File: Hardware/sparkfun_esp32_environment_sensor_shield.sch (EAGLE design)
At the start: 48 parts, among them J1 WEATHER_METER-WIND, J2 WEATHER_METER-RAIN, U1 BME280, U2 CCS811, U3 TSL2561FN, U4 ESD Diode

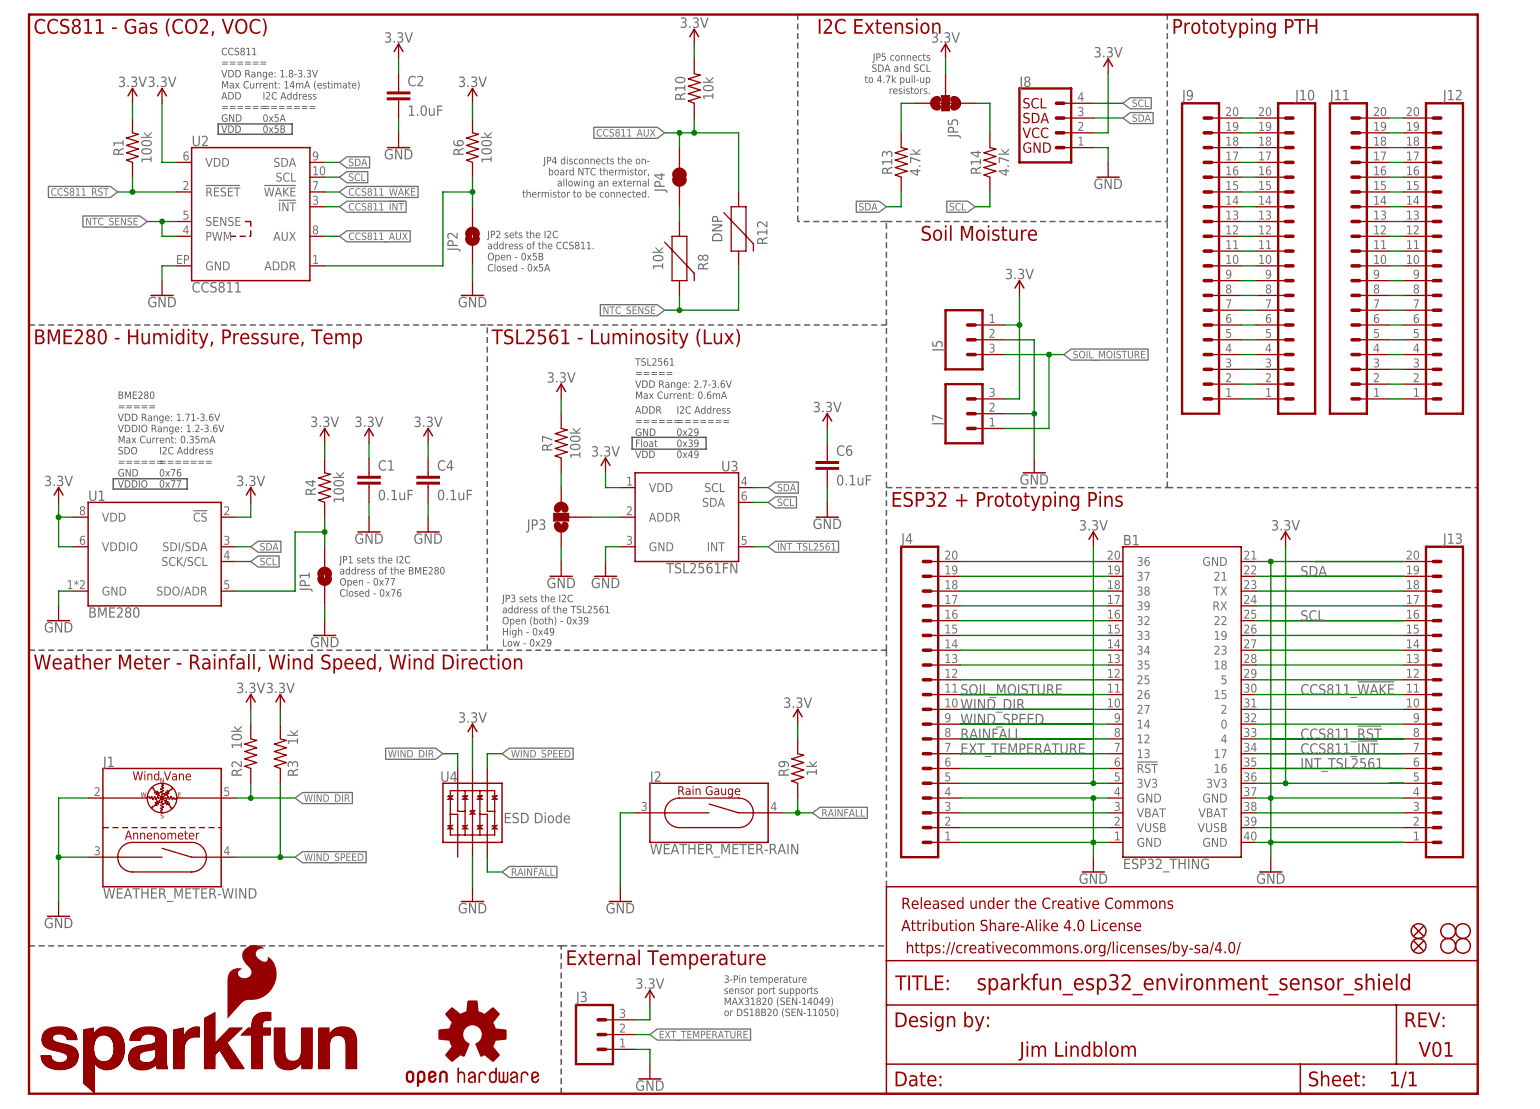
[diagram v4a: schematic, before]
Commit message: Post-review fixes: CCS811 paste, spell check
- Reduced size of CCS811's exposed pad paste aperature
- Fixed anemometer spelling
- Changed "Gas" to "Air" labels
- Clean up schematic
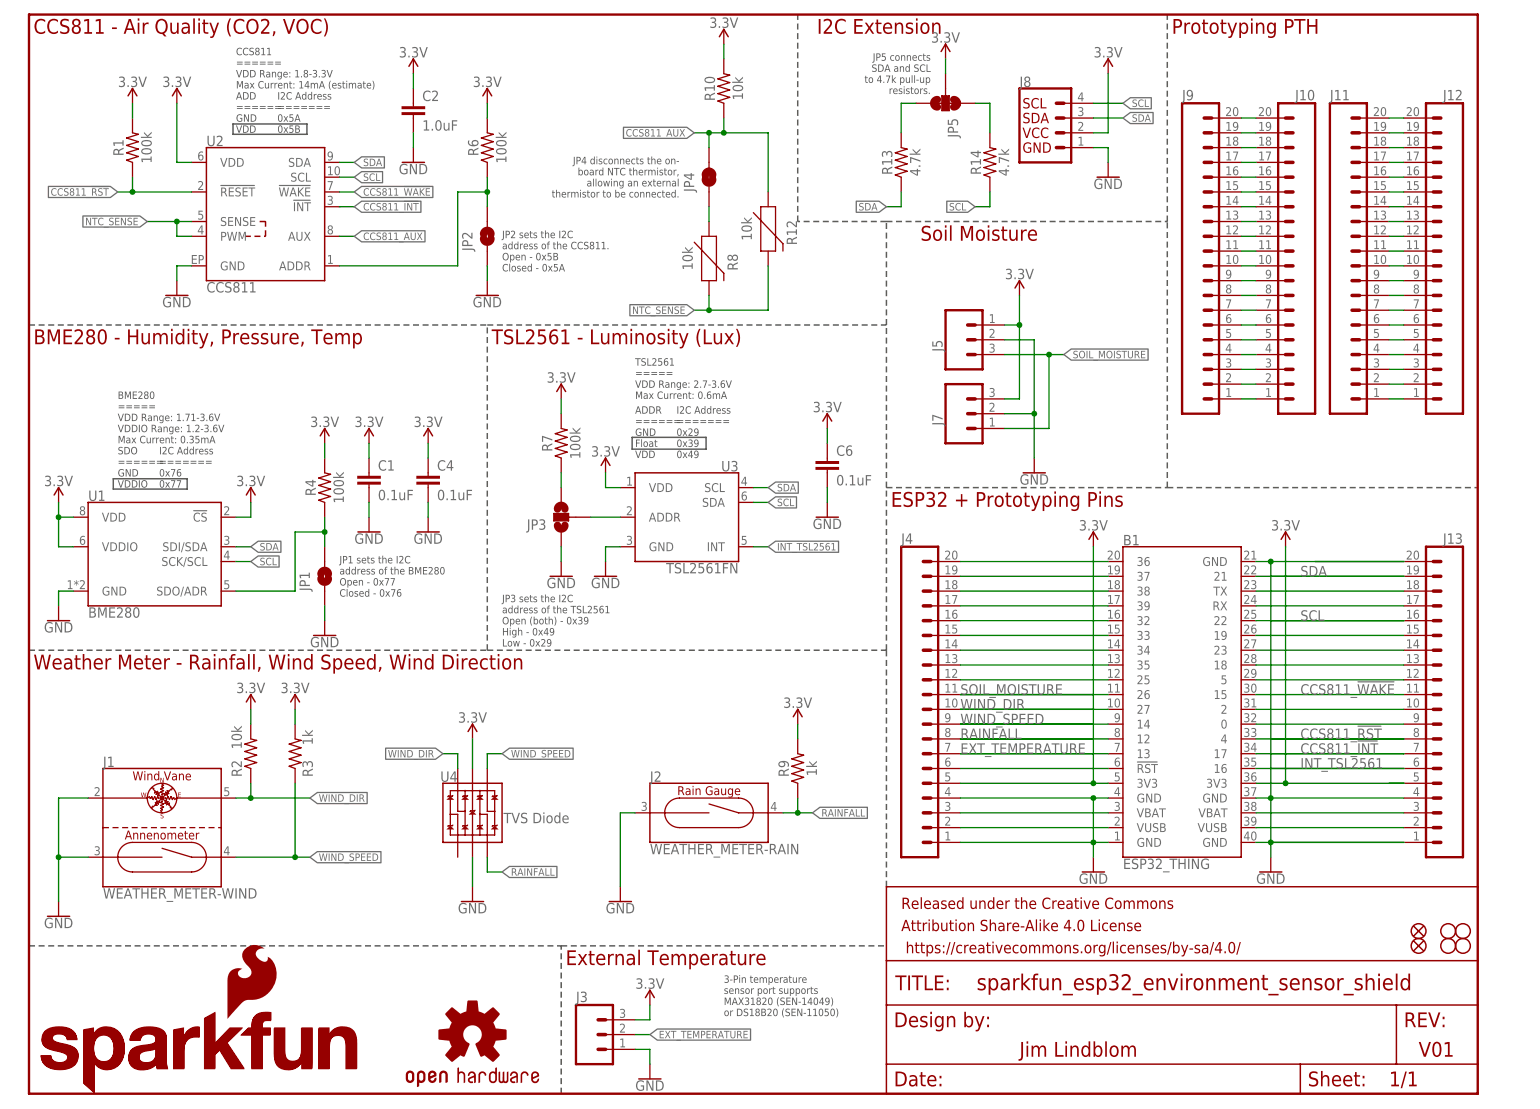
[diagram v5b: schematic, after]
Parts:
- R12: value DNP -> 10k
- U4: value ESD Diode -> TVS Diode
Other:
- note added: "CCS811 - Air Quality (CO2, VOC)"
- note removed: "CCS811 - Gas (CO2, VOC)"
- moved on the sheet: C2, JP2, JP4, R10, R12, R3, R6, R8, U2

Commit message: Minor adjustments after running Engineer checklist.
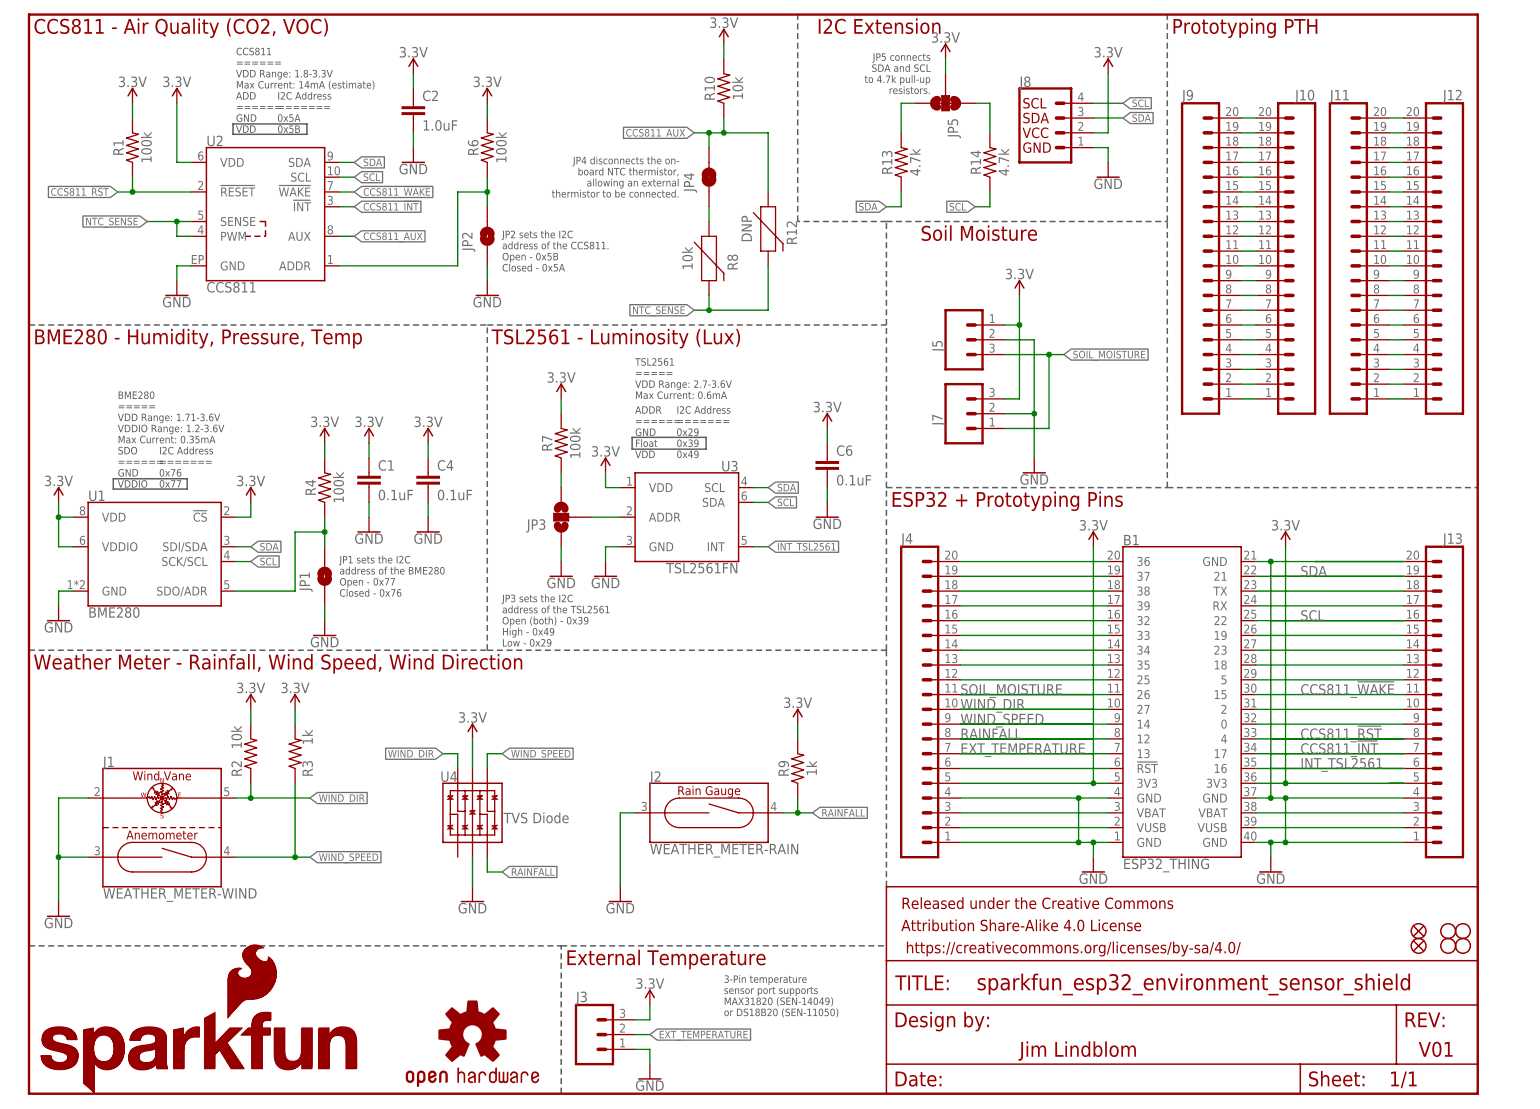
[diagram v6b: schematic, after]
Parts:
- added LOGO3: SFE_LOGO_FLAME.1_INCH, SparkFun-Aesthetics:SFE_LOGO_FLAME.1_INCH
- R12: value 10k -> DNP; PROD_ID (none) -> N/A
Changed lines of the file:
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@@
 <part name="JP5" library="SparkFun-Jumpers" deviceset="JUMPER-SMT_3_2-NC_TRACE" device="_SILK" value=""/>
 <part name="R8" library="esp32-environ-monitor-temp" deviceset="NTC-THERMISTOR" device="-0603" value="10k"/>
-<part name="R12" library="esp32-environ-monitor-temp" deviceset="NTC-THERMISTOR" device="-AXIAL-0.1" value="10k"/>
+<part name="R12" library="esp32-environ-monitor-temp" deviceset="NTC-THERMISTOR" device="-AXIAL-0.1" value="DNP">
+<attribute name="PROD_ID" value="N/A"/>
+</part>
 <part name="LOGO1" library="SparkFun-Aesthetics" deviceset="SFE_LOGO_NAME" device=".1_INCH"/>
 <part name="LOGO4" library="SparkFun-Aesthetics" deviceset="OSHW-LOGO" device="S"/>
@@
 <part name="SUPPLY23" library="SparkFun-PowerSymbols" deviceset="3.3V" device=""/>
 <part name="GND7" library="SparkFun-PowerSymbols" deviceset="GND" device=""/>
+<part name="LOGO3" library="SparkFun-Aesthetics" deviceset="SFE_LOGO_FLAME" device=".1_INCH"/>
 </parts>
 <sheets>
@@
 <instance part="SUPPLY23" gate="G$1" x="76.2" y="60.96"/>
 <instance part="GND7" gate="1" x="76.2" y="33.02" rot="MR0"/>
+<instance part="LOGO3" gate="G$1" x="33.782" y="12.446"/>
 </instances>
 <busses>
@@
 <nets>
 <net name="GND" class="0">
-<segment>
-<pinref part="GND17" gate="1" pin="GND"/>
-<pinref part="B1" gate="G$1" pin="GND@1"/>
-<pinref part="B1" gate="G$1" pin="GND@4"/>
-<pinref part="J4" gate="G$1" pin="1"/>
-<pinref part="J4" gate="G$1" pin="4"/>
-<wire x1="160.02" y1="43.18" x2="182.88" y2="43.18" width="0.1524" layer="91"/>
-<wire x1="182.88" y1="43.18" x2="185.42" y2="43.18" width="0.1524" layer="91"/>
-<wire x1="160.02" y1="50.8" x2="182.88" y2="50.8" width="0.1524" layer="91"/>
-<wire x1="182.88" y1="50.8" x2="185.42" y2="50.8" width="0.1524" layer="91"/>
-<wire x1="182.88" y1="40.64" x2="182.88" y2="43.18" width="0.1524" layer="91"/>
-<junction x="182.88" y="43.18"/>
-<wire x1="182.88" y1="43.18" x2="182.88" y2="50.8" width="0.1524" layer="91"/>
-<junction x="182.88" y="50.8"/>
-</segment>
-<segment>
-<pinref part="B1" gate="G$1" pin="GND@21"/>
-<wire x1="236.22" y1="91.44" x2="220.98" y2="91.44" width="0.1524" layer="91"/>
-<pinref part="J13" gate="G$1" pin="20"/>
-<wire x1="236.22" y1="91.44" x2="213.36" y2="91.44" width="0.1524" layer="91"/>
-<pinref part="B1" gate="G$1" pin="GND@40"/>
-<pinref part="GND19" gate="1" pin="GND"/>
-<wire x1="213.36" y1="91.44" x2="210.82" y2="91.44" width="0.1524" layer="91"/>
-<wire x1="236.22" y1="43.18" x2="213.36" y2="43.18" width="0.1524" layer="91"/>
-<wire x1="213.36" y1="43.18" x2="213.36" y2="40.64" width="0.1524" layer="91"/>
-<pinref part="B1" gate="G$1" pin="GND@37"/>
-<wire x1="213.36" y1="50.8" x2="213.36" y2="43.18" width="0.1524" layer="91"/>
-<junction x="213.36" y="43.18"/>
-<pinref part="J13" gate="G$1" pin="1"/>
-<pinref part="J13" gate="G$1" pin="4"/>
-<wire x1="236.22" y1="43.18" x2="210.82" y2="43.18" width="0.1524" layer="91"/>
-<wire x1="236.22" y1="50.8" x2="213.36" y2="50.8" width="0.1524" layer="91"/>
-<wire x1="213.36" y1="50.8" x2="210.82" y2="50.8" width="0.1524" layer="91"/>
-<wire x1="213.36" y1="91.44" x2="213.36" y2="50.8" width="0.1524" layer="91"/>
-<junction x="213.36" y="91.44"/>
-<junction x="213.36" y="50.8"/>
-</segment>
 <segment>
 <pinref part="GND3" gate="1" pin="GND"/>
@@
 <wire x1="76.2" y1="35.56" x2="76.2" y2="40.64" width="0.1524" layer="91"/>
 </segment>
+<segment>
+<pinref part="B1" gate="G$1" pin="GND@1"/>
+<pinref part="B1" gate="G$1" pin="GND@4"/>
+<pinref part="J4" gate="G$1" pin="1"/>
+<pinref part="J4" gate="G$1" pin="4"/>
+<wire x1="160.02" y1="43.18" x2="180.34" y2="43.18" width="0.1524" layer="91"/>
+<wire x1="180.34" y1="43.18" x2="182.88" y2="43.18" width="0.1524" layer="91"/>
+<wire x1="182.88" y1="43.18" x2="185.42" y2="43.18" width="0.1524" layer="91"/>
+<wire x1="160.02" y1="50.8" x2="180.34" y2="50.8" width="0.1524" layer="91"/>
+<wire x1="180.34" y1="50.8" x2="185.42" y2="50.8" width="0.1524" layer="91"/>
+<junction x="180.34" y="43.18"/>
+<wire x1="180.34" y1="43.18" x2="180.34" y2="50.8" width="0.1524" layer="91"/>
+<junction x="180.34" y="50.8"/>
+<pinref part="GND17" gate="1" pin="GND"/>
+<wire x1="182.88" y1="40.64" x2="182.88" y2="43.18" width="0.1524" layer="91"/>
+<junction x="182.88" y="43.18"/>
+</segment>
+<segment>
+<pinref part="B1" gate="G$1" pin="GND@40"/>
+<pinref part="J13" gate="G$1" pin="1"/>
+<wire x1="236.22" y1="43.18" x2="215.9" y2="43.18" width="0.1524" layer="91"/>
+<wire x1="215.9" y1="43.18" x2="213.36" y2="43.18" width="0.1524" layer="91"/>
+<wire x1="213.36" y1="43.18" x2="210.82" y2="43.18" width="0.1524" layer="91"/>
+<junction x="213.36" y="43.18"/>
+<pinref part="GND19" gate="1" pin="GND"/>
+<wire x1="213.36" y1="40.64" x2="213.36" y2="43.18" width="0.1524" layer="91"/>
+<pinref part="B1" gate="G$1" pin="GND@37"/>
+<pinref part="J13" gate="G$1" pin="4"/>
+<wire x1="236.22" y1="50.8" x2="215.9" y2="50.8" width="0.1524" layer="91"/>
+<pinref part="B1" gate="G$1" pin="GND@21"/>
+<wire x1="215.9" y1="50.8" x2="213.36" y2="50.8" width="0.1524" layer="91"/>
+<wire x1="213.36" y1="50.8" x2="210.82" y2="50.8" width="0.1524" layer="91"/>
+<wire x1="236.22" y1="91.44" x2="220.98" y2="91.44" width="0.1524" layer="91"/>
+<pinref part="J13" gate="G$1" pin="20"/>
+<wire x1="236.22" y1="91.44" x2="213.36" y2="91.44" width="0.1524" layer="91"/>
+<wire x1="213.36" y1="91.44" x2="210.82" y2="91.44" width="0.1524" layer="91"/>
+<wire x1="213.36" y1="91.44" x2="213.36" y2="50.8" width="0.1524" layer="91"/>
+<junction x="213.36" y="91.44"/>
+<junction x="213.36" y="50.8"/>
+<wire x1="215.9" y1="43.18" x2="215.9" y2="50.8" width="0.1524" layer="91"/>
+<junction x="215.9" y="43.18"/>
+<junction x="215.9" y="50.8"/>
+</segment>
 </net>

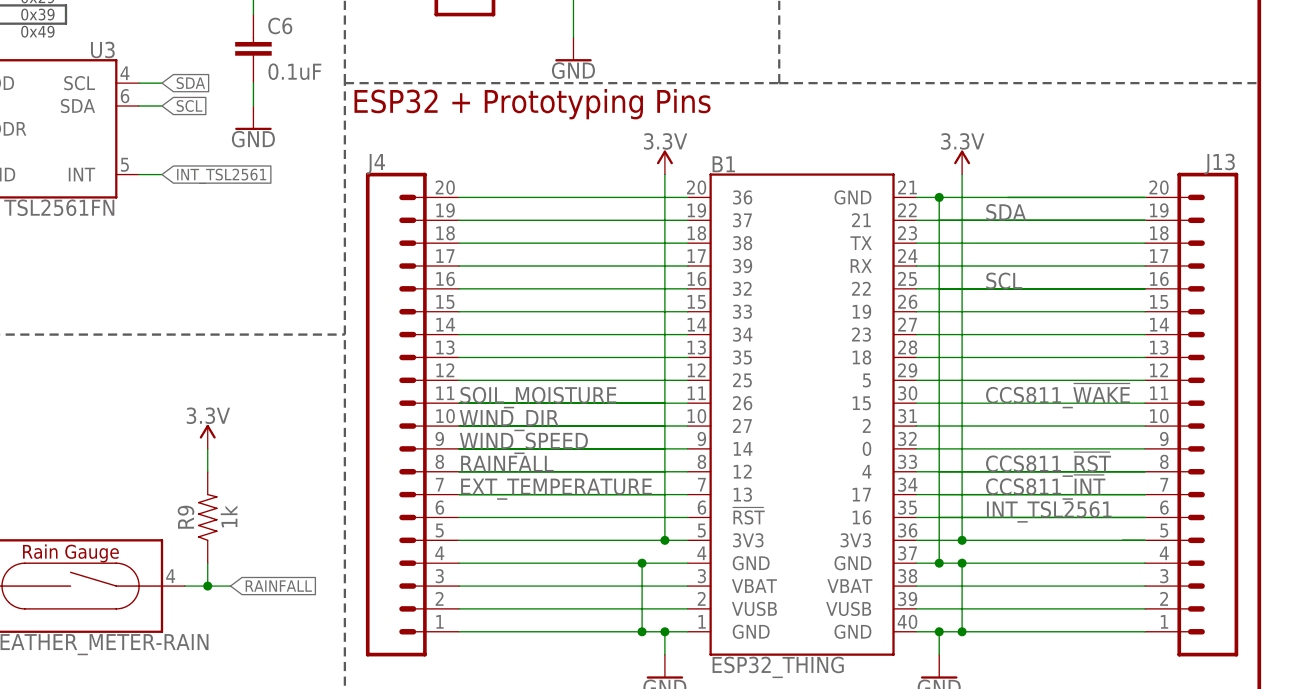
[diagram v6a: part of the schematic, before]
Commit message: Adjustin silkscreen, adding measures to RJ11 jacks, screw terminals.
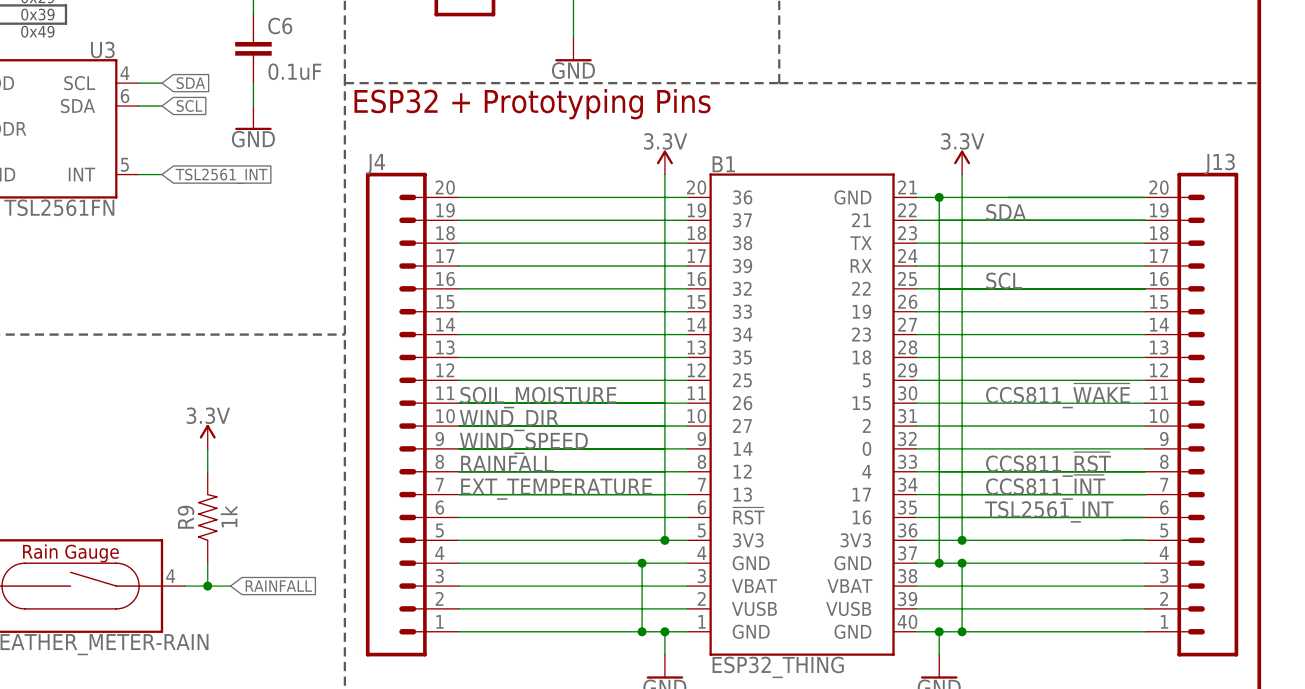
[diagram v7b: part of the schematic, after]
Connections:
- net INT_TSL2561 renamed TSL2561_INT
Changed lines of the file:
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@@
 </segment>
 </net>
-<net name="INT_TSL2561" class="0">
+<net name="TSL2561_INT" class="0">
 <segment>
 <pinref part="U3" gate="G$1" pin="INT"/>
